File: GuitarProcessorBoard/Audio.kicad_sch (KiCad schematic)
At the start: 31 parts, among them U201 TLV320AIC3204, U202 TL074

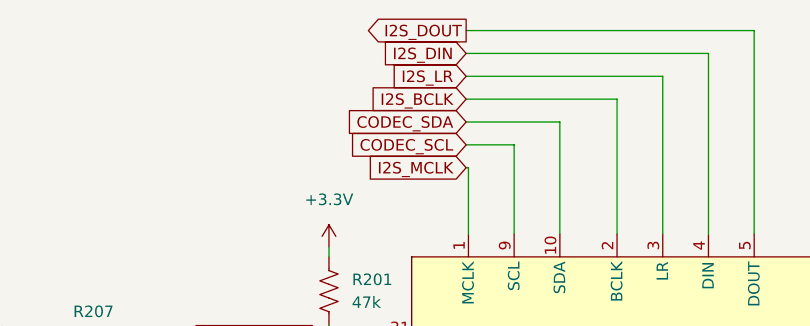
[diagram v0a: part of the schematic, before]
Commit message: basic MCU pinout, IO headers
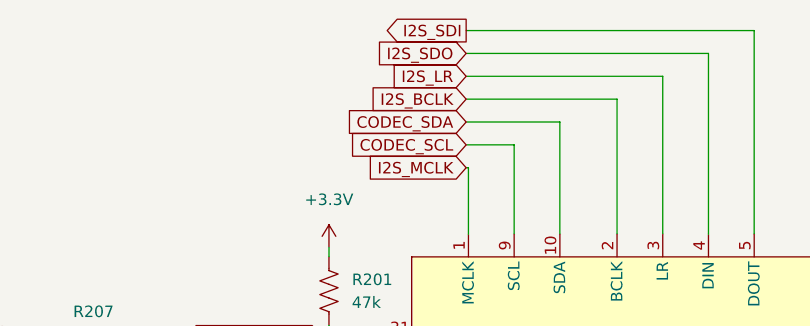
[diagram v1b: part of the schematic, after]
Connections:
- net I2S_DIN renamed I2S_SDO
- net I2S_DOUT renamed I2S_SDI
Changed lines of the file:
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@@
 		)
 	)
-	(global_label "I2S_DOUT"
+	(global_label "I2S_SDI"
 		(shape output)
 		(at 128.524 36.576 180)
@@
 		)
 		(property "Intersheetrefs" "${INTERSHEET_REFS}"
-			(at 116.6488 36.576 0)
+			(at 118.4631 36.576 0)
 			(effects
 				(font
@@
 		)
 	)
-	(global_label "I2S_DIN"
+	(global_label "I2S_SDO"
 		(shape input)
 		(at 128.524 39.116 180)
@@
 		)
 		(property "Intersheetrefs" "${INTERSHEET_REFS}"
-			(at 118.3421 39.116 0)
+			(at 117.7374 39.116 0)
 			(effects
 				(font

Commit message: control wiring
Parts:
- removed RV201: 100kA, symbol Device:R_Potentiometer_US
- removed unit 3 of U202
- added R214: 10k, symbol Device:R_US
- C209, C214: value 100n -> 1u
- R211: value 10k -> 100k
- R212: value 47k -> 470k
- R213: value 220 -> 10k
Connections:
- net FX_OUT: now also R213.2, R214.1
- net GND: now also R214.2
- net at C215.1: now also R212.2, U202.14; no longer R213.2
- net at C215.2: now also R213.1
- no-connect marks 14 -> 11
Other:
- note removed: "Output Volume"
- moved on the sheet: C215

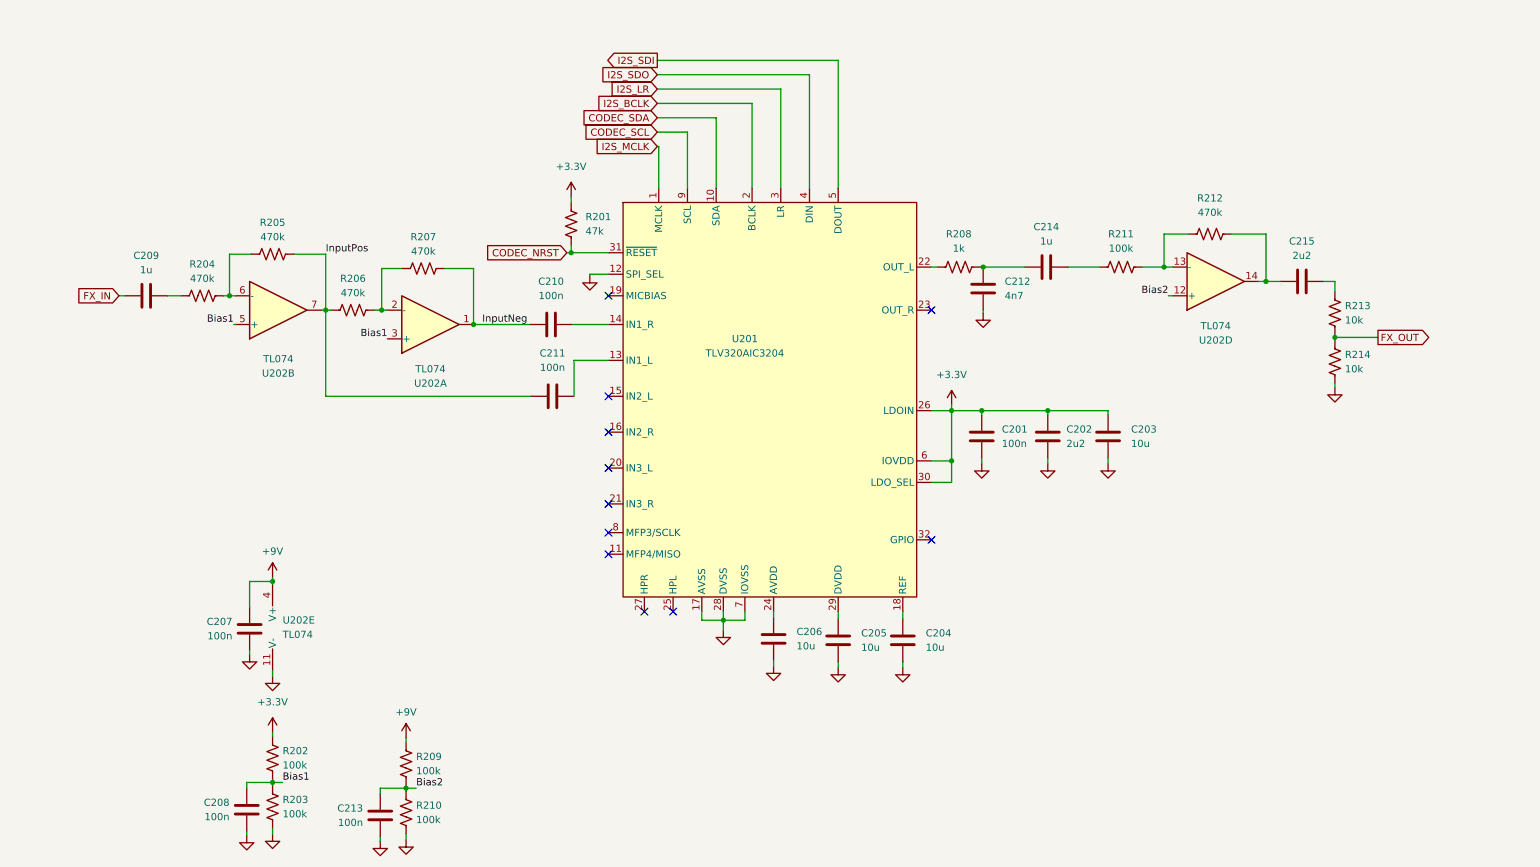
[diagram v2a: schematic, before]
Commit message: added analog wet/dry control
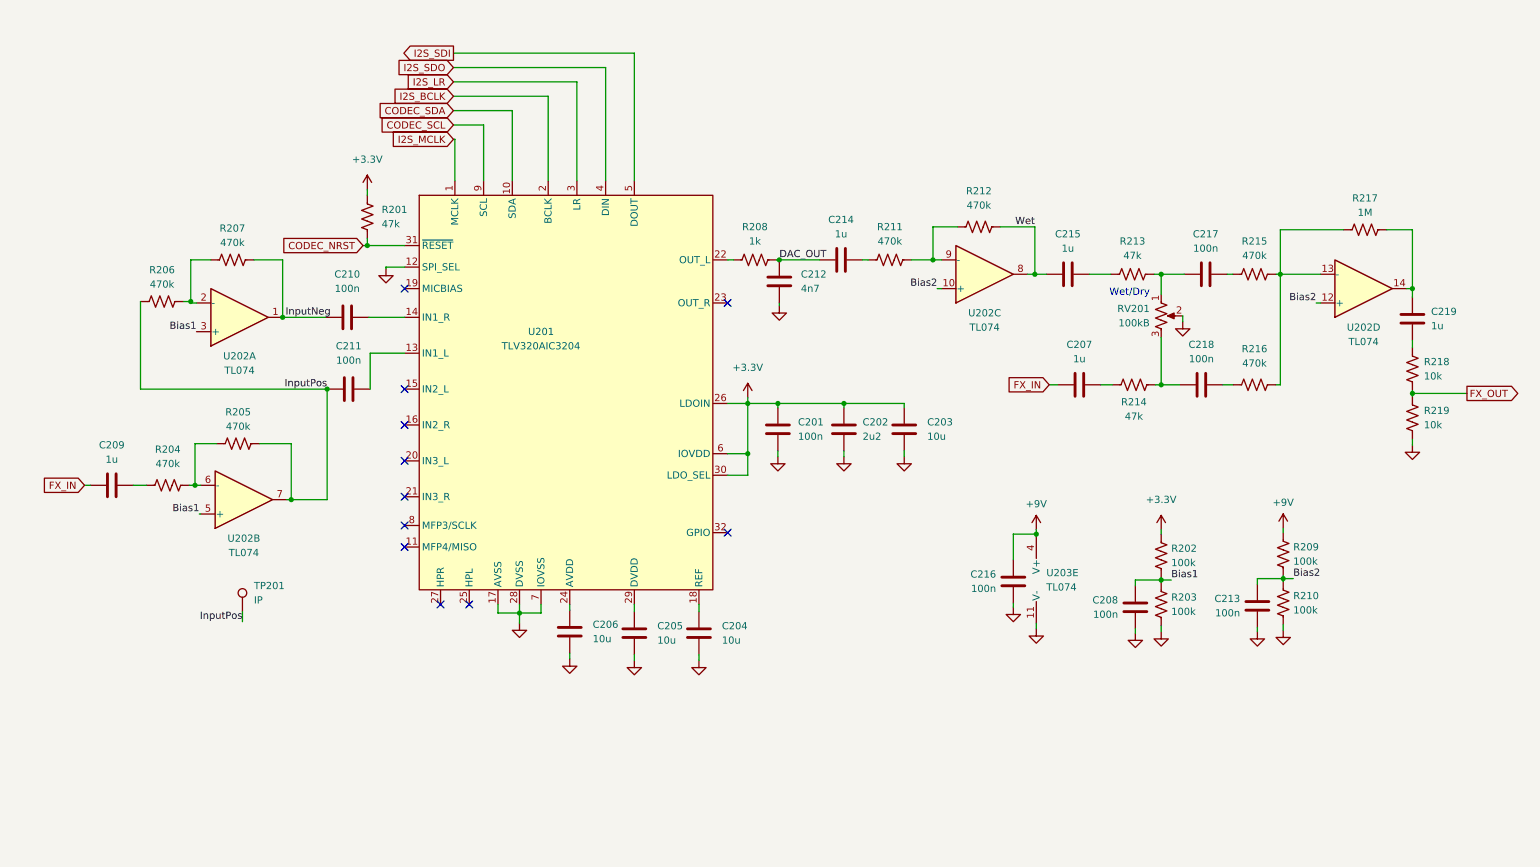
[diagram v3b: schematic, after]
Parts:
- removed unit 5 of U202
- added C216, C217, C218: 100n, symbol Device:C
- added C219: 1u, symbol Device:C
- added R215, R216: 470k, symbol Device:R_US
- added R217: 1M, symbol Device:R_US
- added R218, R219: 10k, symbol Device:R_US
- added RV201: 100kB, symbol Device:R_Potentiometer_US
- added TP201: IP, TestPoint:TestPoint_THTPad_D2.0mm_Drill1.0mm_VAL, symbol Connector:TestPoint
- added unit 3 of U202
- added U203: TL074, symbol Amplifier_Operational:TL074
- C207: value 100n -> 1u
- C215: value 2u2 -> 1u
- R211: value 100k -> 470k
- R213, R214: value 10k -> 47k
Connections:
- net +9V: now also C216.1, U203.4 (V+); no longer C207.1
- net Bias2: now also U202.10 (+)
- net FX_IN: now also C207.1
- net FX_OUT: now also R218.2, R219.1; no longer R213.2, R214.1
- net GND: now also C216.2, R219.2, RV201.2, U203.11 (V-); no longer C207.2, R214.2
- net InputPos: now also TP201.1
- net DAC_OUT: now reaches C212.1, C214.1, R208.2
- net Wet: now reaches C215.1, R212.2
- net Wet: now also U202.8; no longer U202.14
- net at R211.2, R212.1: now also U202.9 (-); no longer U202.13 (-)
- new net: C217.1, R213.2, RV201.1
- new net: C219.2, R218.1
- new net: C207.2, R214.1
- new net: C218.1, R214.2, RV201.3
- new net: R215.2, R216.2, R217.1, U202.13 (-)
- new net: C219.1, R217.2, U202.14
- new net: C217.2, R215.1
- new net: C218.2, R216.1
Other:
- note added: "Wet/Dry"
- moved on the sheet: C201, C202, C203, C204, C205, C206, C208, C209, C210, C211, C212, C213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

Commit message: control/ enclosure layout
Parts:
- added TP202: DAC, TestPoint:TestPoint_THTPad_D2.0mm_Drill1.0mm_VAL, symbol Connector:TestPoint
- added TP203: WET, TestPoint:TestPoint_THTPad_D2.0mm_Drill1.0mm_VAL, symbol Connector:TestPoint
- C201, C202, C203, C204, C205, C206, C207, C208, C209, C210, C211, C212, C213, C214, C215, C216, C217, C218, C219: footprint (none) -> Capacitor_SMD:C_0805_2012Metric
- R201, R202, R203, R204, R205, R206, R207, R208, R209, R210, R211, R212, R213, R214, R215, R216, R217, R218, R219: footprint (none) -> Resistor_SMD:R_0805_2012Metric
- RV201: footprint (none) -> Potentiometer_THT:Potentiometer_Alpha_RV16AF_42_Single_Long
- U202: footprint (none) -> Package_SO:SOIC-14_3.9x8.7mm_P1.27mm
- U202: renamed from U203; footprint (none) -> Package_SO:SOIC-14_3.9x8.7mm_P1.27mm
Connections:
- net DAC_OUT: now also R208.1, U201.22 (OUT_L), TP202.1; no longer C212.1, C214.1, R208.2
- net Wet: now also TP203.1
- new net: C212.1, C214.1, R208.2

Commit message: starting layout
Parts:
- removed C208, C213: 100n, Capacitor_SMD:C_0805_2012Metric, symbol Device:C
- added R220: 22, Resistor_SMD:R_0805_2012Metric, symbol Device:R_US
- RV201: footprint Potentiometer_THT:Potentiometer_Alpha_RV16AF_42_Single_Long -> Potentiometer_THT:Potentiometer_Alpha_RD901F-40-00D_Single_Vertical_CircularHoles
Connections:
- net Bias1: now also U202.10 (+), U202.12 (+); no longer U202.3 (+), U202.5 (+)
- net Bias2: now also U202.3 (+), U202.5 (+); no longer U202.10 (+), U202.12 (+)
- net I2S_SDI: now also R220.1; no longer U201.5 (DOUT)
- net InputNeg: now also U202.8; no longer U202.1
- net InputPos: now also U202.14; no longer U202.7
- net Wet: now also U202.7; no longer U202.8
- net at R206.2, R207.1: now also U202.9 (-); no longer U202.2 (-)
- net at R204.2, R205.1: now also U202.13 (-); no longer U202.6 (-)
- net at R211.2, R212.1: now also U202.6 (-); no longer U202.9 (-)
- net at R215.2, R216.2, R217.1: now also U202.2 (-); no longer U202.13 (-)
- net at C219.1, R217.2: now also U202.1; no longer U202.14
- new net: R220.2, U201.5 (DOUT)
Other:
- moved on the sheet: U202A, U202B, U202C, U202D

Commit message: first layout
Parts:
- removed TP201: IP, TestPoint:TestPoint_THTPad_D2.0mm_Drill1.0mm_VAL, symbol Connector:TestPoint
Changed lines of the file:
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@@
 	(wire
 		(pts
-			(xy 55.118 134.112) (xy 55.118 135.89)
-		)
-		(stroke
-			(width 0)
-			(type default)
-		)
-	)
-	(wire
-		(pts
 			(xy 177.292 71.882) (xy 178.816 71.882)
 		)
@@
 		)
 	)
-	(label "InputPos"
-		(at 55.118 135.89 180)
-		(fields_autoplaced yes)
-		(effects
-			(font
-				(size 1.27 1.27)
-			)
-			(justify right bottom)
-		)
-	)
 	(label "Wet"
 		(at 195.326 66.04 180)
@@
 					(unit 1)
 				)
-			)
-		)
-	)
-	(symbol
-		(lib_id "Connector:TestPoint")
-		(at 55.118 134.112 0)
-		(unit 1)
-		(exclude_from_sim no)
-		(in_bom no)
-		(on_board yes)
-		(dnp no)
-		(fields_autoplaced yes)
-		(property "Reference" "TP201"
-			(at 57.15 129.5399 0)
-			(effects
-				(font
-					(size 1.27 1.27)
-				)
-				(justify left)
-			)
-		)
-		(property "Value" "IP"
-			(at 57.15 132.0799 0)
-			(effects
-				(font
-					(size 1.27 1.27)
-				)
-				(justify left)
-			)
-		)
-		(property "Footprint" "TestPoint:TestPoint_THTPad_D2.0mm_Drill1.0mm_VAL"
-			(at 60.198 134.112 0)
-			(effects
-				(font
-					(size 1.27 1.27)
-				)
-				(hide yes)
-			)
-		)
-		(property "Datasheet" "~"
-			(at 60.198 134.112 0)
-			(effects
-				(font
-					(size 1.27 1.27)
-				)
-				(hide yes)
-			)
-		)
-		(property "Description" "test point"
-			(at 55.118 134.112 0)
-			(effects
-				(font
-					(size 1.27 1.27)
-				)
-				(hide yes)
-			)
-		)
-		(pin "1"
-		)
-		(instances
-			(project "GuitarProcessorBoard"
-				(path "/524c695b-c632-4089-9e9a-ef0f89cad1b2/ef3a9a4a-abe1-4d77-855c-3594c7f88930"
-					(reference "TP201")
-					(unit 1)
-				)

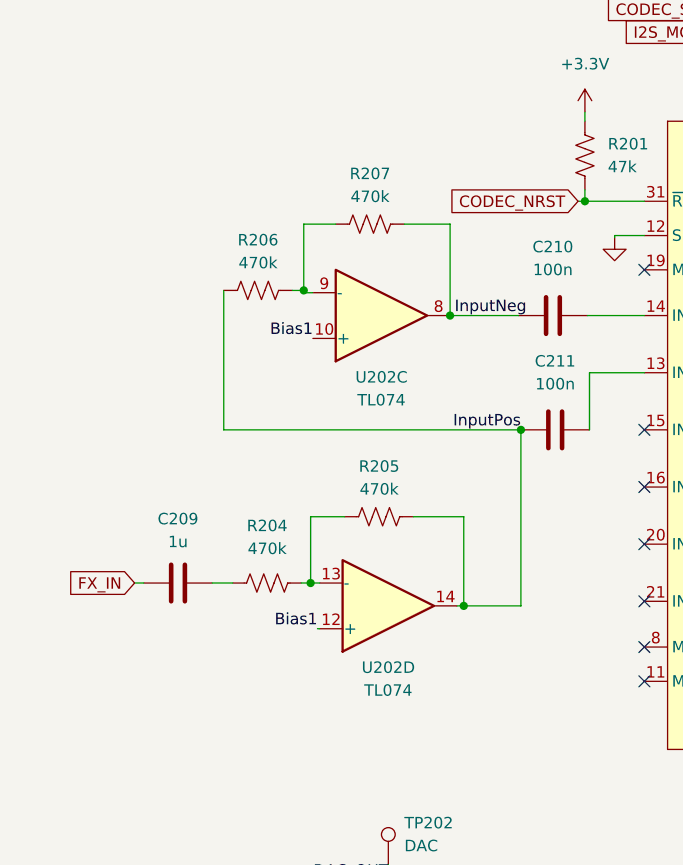
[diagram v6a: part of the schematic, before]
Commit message: processing callback set up
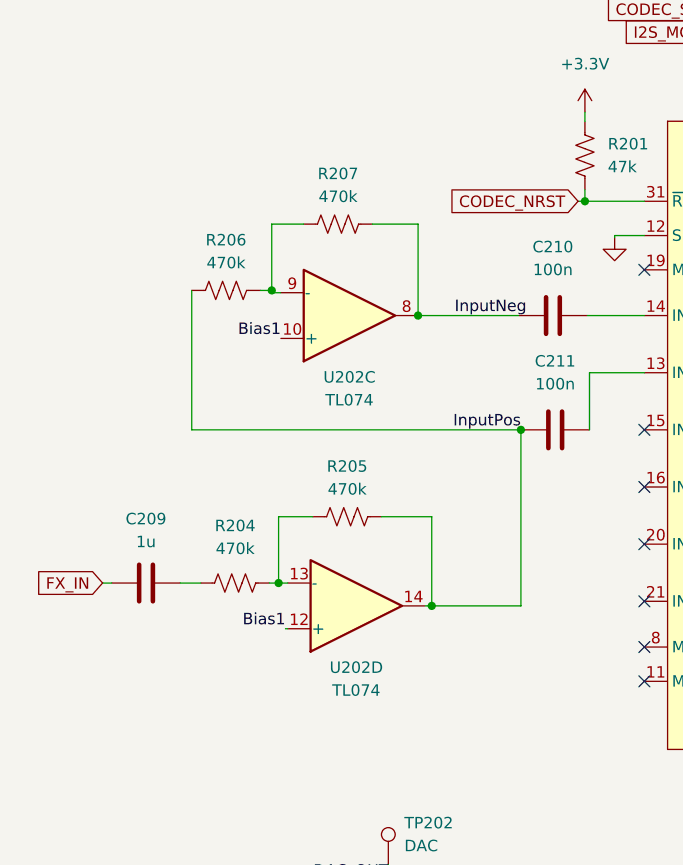
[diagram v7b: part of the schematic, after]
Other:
- moved on the sheet: C209, R204, R205, R206, R207, U202C, U202D
